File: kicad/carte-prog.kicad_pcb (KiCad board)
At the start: 2 copper layers, 67.9 x 19.7 mm, 5 parts, among them J1 Connecteur côté carte, J2 RJ12 - Côté ordinateur, J3 3.3V, J4 5V, J5 ALIM

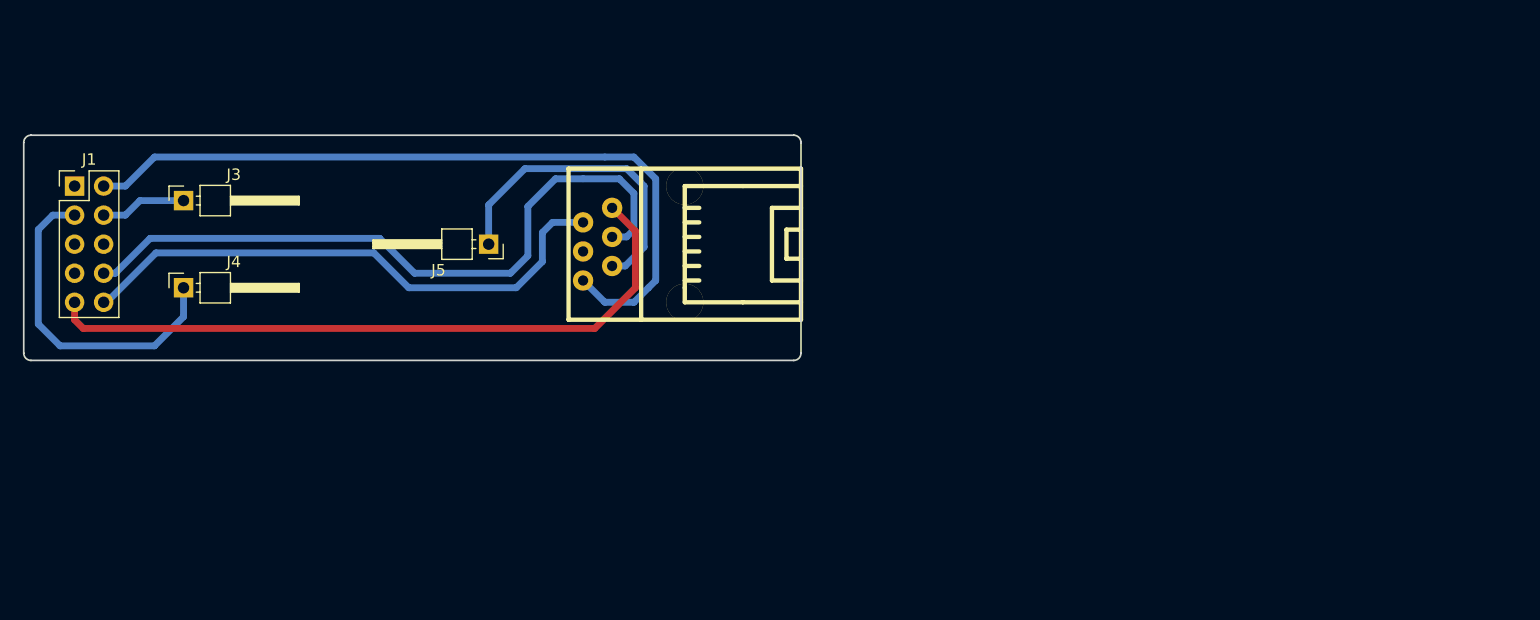
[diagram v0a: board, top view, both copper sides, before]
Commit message: Ajout d'un max232
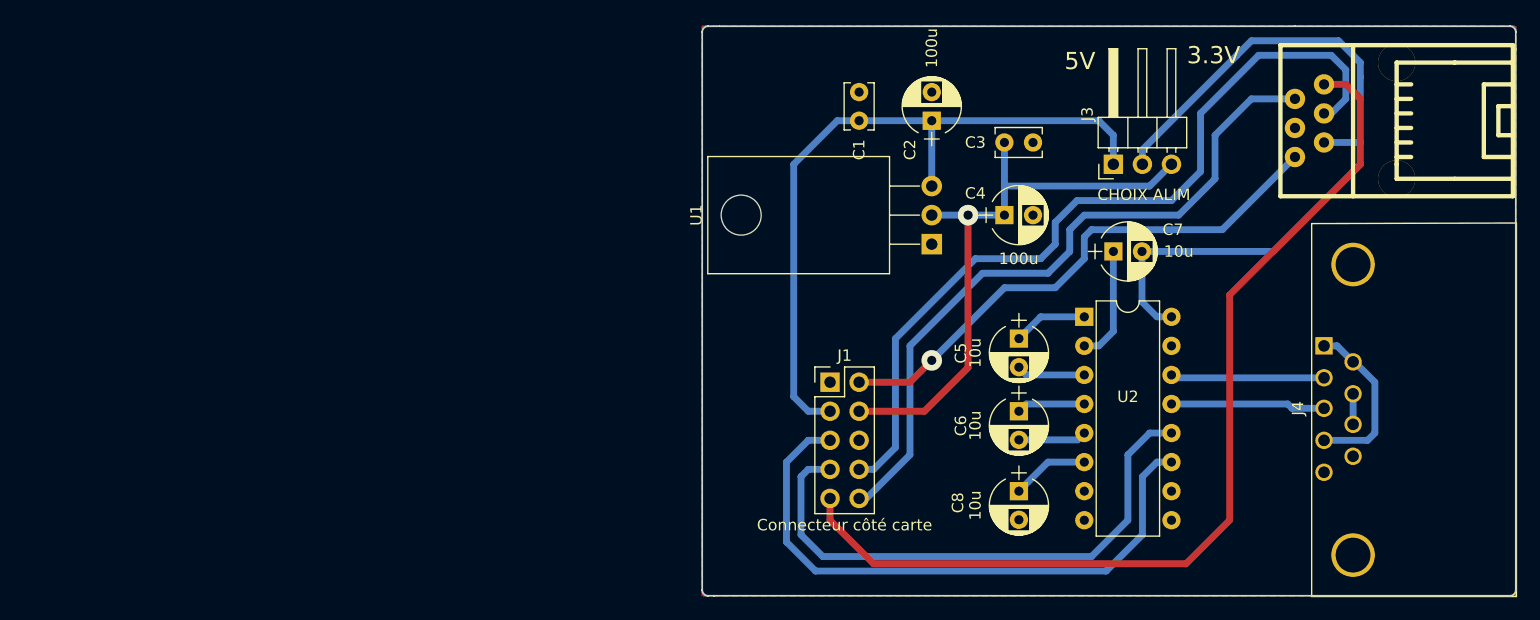
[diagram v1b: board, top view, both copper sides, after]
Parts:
- removed J5: ALIM, Pin_Headers:Pin_Header_Angled_1x01_Pitch2.54mm
- added C1: 100n, Capacitors_THT:C_Rect_L4.0mm_W2.5mm_P2.50mm, F.Cu at (200.7, 94.6)
- added C2: 100u, Capacitors_THT:CP_Radial_D5.0mm_P2.50mm, F.Cu at (207.0, 94.6)
- added C3: 100n, Capacitors_THT:C_Rect_L4.0mm_W2.5mm_P2.50mm, F.Cu at (213.4, 96.5)
- added C4: 100u, Capacitors_THT:CP_Radial_D5.0mm_P2.50mm, F.Cu at (213.4, 102.9)
- added C5: 10u, Capacitors_THT:CP_Radial_D5.0mm_P2.50mm, F.Cu at (214.6, 113.7)
- added C6: 10u, Capacitors_THT:CP_Radial_D5.0mm_P2.50mm, F.Cu at (214.6, 120.0)
- added C7: 10u, Capacitors_THT:CP_Radial_D5.0mm_P2.50mm, F.Cu at (222.9, 106.0)
- added C8: 10u, Capacitors_THT:CP_Radial_D5.0mm_P2.50mm, F.Cu at (214.6, 127.0)
- added U1: LM1117-3.3, TO_SOT_Packages_THT:TO-220_Horizontal, F.Cu at (207.0, 105.4)
- added U2: MAX232, Housings_DIP:DIP-16_W7.62mm, F.Cu at (220.3, 111.8)
- J3: value 3.3V -> CHOIX ALIM; footprint Pin_Headers:Pin_Header_Angled_1x01_Pitch2.54mm -> Pin_Headers:Pin_Header_Angled_1x03_Pitch2.54mm
- J4: value 5V -> DB9_Female; footprint Pin_Headers:Pin_Header_Angled_1x01_Pitch2.54mm -> Connectors:DB9FC
- moved J4 99.8 mm to (241.3, 114.3), turned to 270 degrees
- moved J3 81.3 mm to (222.9, 98.4), turned to 90 degrees
- moved J1 68.2 mm to (198.1, 117.5)
- moved J2 63.2 mm to (247.7, 94.6)
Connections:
- J1 pad 5: (no net) -> /DBG_TX
- J1 pad 7: (no net) -> /DBG_RX
- J3 pad 1: +3V3 -> +5V
- J4 pad 1: +5V -> Net-(J4-Pad1)
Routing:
- net /DBG_TX: track 0.00 -> 53.2 mm
- net /DBG_RX: track 0.00 -> 48.9 mm
- net +3V3: track 7.51 -> 52.5 mm, vias 0 -> 1
- net /ALIM: track 27.8 -> 66.9 mm
- net +5V: track 29.0 -> 62.3 mm
- net /PDB: track 60.2 -> 85.3 mm
- net /MCLR: track 66.9 -> 47.4 mm, vias 0 -> 1
- net Net-(J4-Pad1): track 0.00 -> 14.9 mm
- net Net-(J4-Pad3): track 0.00 -> 13.5 mm
- net Net-(J4-Pad2): track 0.00 -> 13.4 mm
- net /PCK: track 48.8 -> 61.5 mm
- net /PDT: track 60.7 -> 72.7 mm
- net Net-(C7-Pad1): track 0.00 -> 10.1 mm
- net Net-(C8-Pad1): track 0.00 -> 6.77 mm
- net Net-(C5-Pad1): track 0.00 -> 6.50 mm
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- added copper zone on B.Cu, net GND
- added copper zone on F.Cu, net GND
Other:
- board size 67.9 x 19.7 mm -> 71.1 x 49.8 mm
- net class Default: via_dia 0.6 -> 1.8; via_drill 0.4 -> 0.8
- board text added: "3.3V"
- board text added: "5V"

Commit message: Modification des caches
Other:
- board text added: "Prog"
- board text added: "v X.X"
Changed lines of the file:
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@@
     (area 185.455 86.184047 267.175001 136.615001)
     (thickness 1.6)
-    (drawings 14)
+    (drawings 16)
     (tracks 130)
     (zones 0)
@@
   )
   (page A4)
+  (title_block
+    (title "Carte programmation")
+    (rev vx.x)
+    (company "Ecole Centrale Lyon")
+    (comment 1 "Année 2018")
+    (comment 2 "Contacter G. CHARREAUX")
+    (comment 3 chxguillaume@gmail.com)
+  )
   (layers
     (0 F.Cu signal)
@@
     )
   )
+  (gr_text Prog (at 191.516 89.916) (layer F.SilkS)
+    (effects (font (size 1.5 1.5) (thickness 0.3)))
+  )
+  (gr_text "v X.X" (at 192.024 92.456) (layer F.SilkS)
+    (effects (font (size 1.5 1.5) (thickness 0.3)))
+  )
   (gr_text 3.3V (at 231.648 88.9) (layer F.SilkS)

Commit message: Modification des cartouches en vue de la release
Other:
- board text added: "v 1.0"
- board text removed: "v X.X"
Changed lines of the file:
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@@
   (title_block
     (title "Carte programmation")
-    (rev vx.x)
+    (date 2018-04-22)
+    (rev v1.0)
     (company "Ecole Centrale Lyon")
     (comment 1 "Année 2018")
@@
     (effects (font (size 1.5 1.5) (thickness 0.3)))
   )
-  (gr_text "v X.X" (at 192.024 92.456) (layer F.SilkS)
+  (gr_text "v 1.0" (at 192.024 92.456) (layer F.SilkS)
     (effects (font (size 1.5 1.5) (thickness 0.3)))
   )
